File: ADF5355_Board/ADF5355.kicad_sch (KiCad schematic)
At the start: 20 parts

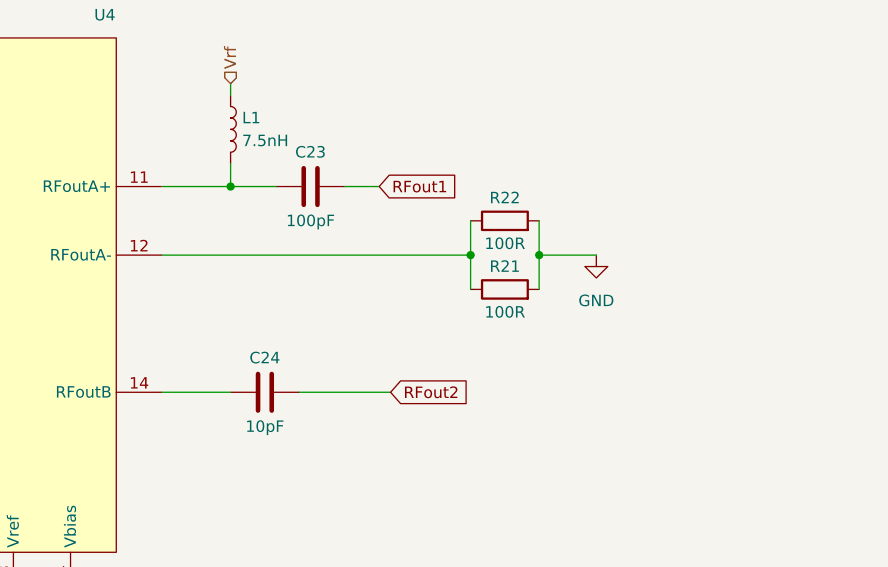
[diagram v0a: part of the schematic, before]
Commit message: Finished MCU board
Finished MCU board and started finishing up the VCO board
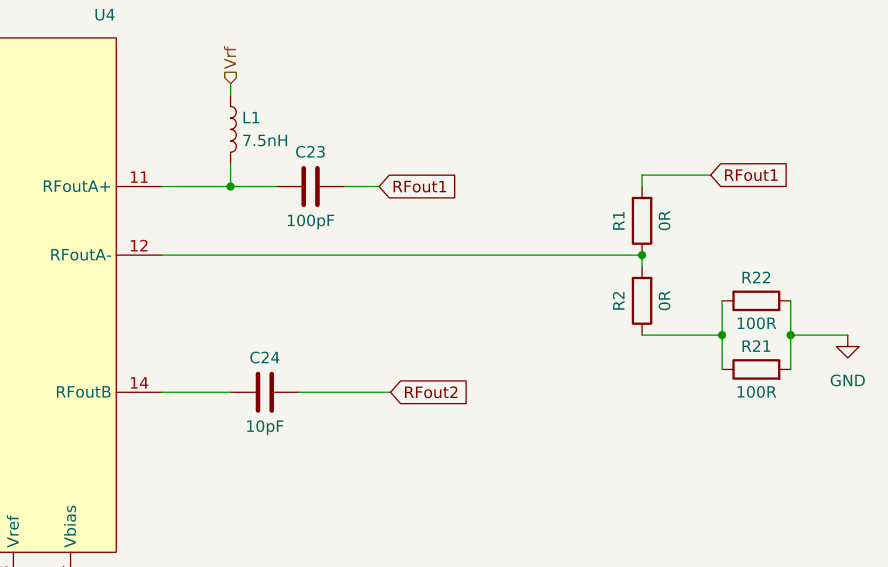
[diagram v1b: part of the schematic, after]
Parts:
- added R1, R2: 0R, symbol Device:R
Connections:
- net RFout1: now also R1.2
- net at R21.1, R22.1: now also R2.1; no longer U4.12 (RFoutA-)
- new net: R1.1, R2.2, U4.12 (RFoutA-)
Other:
- moved on the sheet: R21, R22
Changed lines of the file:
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@@
   (junction (at 156.21 139.7) (diameter 0) (color 0 0 0 0)
   )
-  (junction (at 219.71 85.09) (diameter 0) (color 0 0 0 0)
+  (junction (at 240.03 93.98) (diameter 0) (color 0 0 0 0)
+  )
+  (junction (at 247.65 93.98) (diameter 0) (color 0 0 0 0)
   )
   (junction (at 146.05 123.19) (diameter 0) (color 0 0 0 0)
@@
   (junction (at 185.42 77.47) (diameter 0) (color 0 0 0 0)
   )
+  (junction (at 231.14 85.09) (diameter 0) (color 0 0 0 0)
+  )
   (junction (at 138.43 123.19) (diameter 0) (color 0 0 0 0)
   )
@@
   (junction (at 140.97 123.19) (diameter 0) (color 0 0 0 0)
   )
-  (junction (at 212.09 85.09) (diameter 0) (color 0 0 0 0)
-  )
   (junction (at 54.61 101.6) (diameter 0) (color 0 0 0 0)
   )
@@
     (stroke (width 0) (type default))
   )
-  (wire (pts (xy 177.8 85.09) (xy 212.09 85.09))
-    (stroke (width 0) (type default))
-  )
   (wire (pts (xy 143.51 55.88) (xy 146.05 55.88))
     (stroke (width 0) (type default))
@@
     (stroke (width 0) (type default))
   )
+  (wire (pts (xy 231.14 86.36) (xy 231.14 85.09))
+    (stroke (width 0) (type default))
+  )
+  (wire (pts (xy 231.14 93.98) (xy 240.03 93.98))
+    (stroke (width 0) (type default))
+  )
   (wire (pts (xy 43.18 96.52) (xy 43.18 101.6))
     (stroke (width 0) (type default))
   )
-  (wire (pts (xy 219.71 85.09) (xy 226.06 85.09))
+  (wire (pts (xy 247.65 93.98) (xy 254 93.98))
     (stroke (width 0) (type default))
   )
@@
     (stroke (width 0) (type default))
   )
-  (wire (pts (xy 212.09 81.28) (xy 212.09 85.09))
-    (stroke (width 0) (type default))
-  )
-  (wire (pts (xy 219.71 81.28) (xy 219.71 85.09))
+  (wire (pts (xy 247.65 90.17) (xy 247.65 93.98))
     (stroke (width 0) (type default))
   )
@@
     (stroke (width 0) (type default))
   )
+  (wire (pts (xy 238.76 76.2) (xy 231.14 76.2))
+    (stroke (width 0) (type default))
+  )
   (wire (pts (xy 71.12 66.04) (xy 71.12 90.17))
     (stroke (width 0) (type default))
@@
     (stroke (width 0) (type default))
   )
-  (wire (pts (xy 212.09 85.09) (xy 212.09 88.9))
-    (stroke (width 0) (type default))
-  )
   (wire (pts (xy 181.61 139.7) (xy 181.61 135.89))
     (stroke (width 0) (type default))
@@
     (stroke (width 0) (type default))
   )
+  (wire (pts (xy 240.03 93.98) (xy 240.03 97.79))
+    (stroke (width 0) (type default))
+  )
   (wire (pts (xy 96.52 74.93) (xy 105.41 74.93))
     (stroke (width 0) (type default))
@@
     (stroke (width 0) (type default))
   )
-  (wire (pts (xy 219.71 85.09) (xy 219.71 88.9))
+  (wire (pts (xy 247.65 93.98) (xy 247.65 97.79))
     (stroke (width 0) (type default))
   )
@@
     (stroke (width 0) (type default))
   )
+  (wire (pts (xy 231.14 76.2) (xy 231.14 77.47))
+    (stroke (width 0) (type default))
+  )
   (wire (pts (xy 63.5 81.28) (xy 63.5 85.09))
     (stroke (width 0) (type default))
@@
     (stroke (width 0) (type default))
   )
+  (wire (pts (xy 231.14 85.09) (xy 177.8 85.09))
+    (stroke (width 0) (type default))
+  )
   (wire (pts (xy 130.81 46.99) (xy 135.89 46.99))
+    (stroke (width 0) (type default))
+  )
+  (wire (pts (xy 240.03 90.17) (xy 240.03 93.98))
     (stroke (width 0) (type default))
   )
@@
     (effects (font (size 1.27 1.27)) (justify left))
     (property "Intersheetrefs" "${INTERSHEET_REFS}" (at 212.0434 100.33 0)
+      (effects (font (size 1.27 1.27)) (justify left) hide)
+    )
+  )
+  (global_label "RFout1" (shape input) (at 238.76 76.2 0) (fields_autoplaced)
+    (effects (font (size 1.27 1.27)) (justify left))
+    (property "Intersheetrefs" "${INTERSHEET_REFS}" (at 247.6034 76.2 0)
       (effects (font (size 1.27 1.27)) (justify left) hide)
     )
@@
     )
   )
-  (symbol (lib_id "Device:R") (at 215.9 88.9 90) (unit 1)
-    (in_bom yes) (on_board yes) (dnp no)
-    (property "Reference" "R21" (at 215.9 86.36 90)
-      (effects (font (size 1.27 1.27)))
-    )
-    (property "Value" "100R" (at 215.9 91.44 90)
-      (effects (font (size 1.27 1.27)))
-    )
-    (property "Footprint" "Resistor_SMD:R_0603_1608Metric_Pad0.98x0.95mm_HandSolder" (at 215.9 90.678 90)
-      (effects (font (size 1.27 1.27)) hide)
-    )
-    (property "Datasheet" "~" (at 215.9 88.9 0)
+  (symbol (lib_id "Device:R") (at 243.84 97.79 90) (unit 1)
+    (in_bom yes) (on_board yes) (dnp no)
+    (property "Reference" "R21" (at 243.84 95.25 90)
+      (effects (font (size 1.27 1.27)))
+    )
+    (property "Value" "100R" (at 243.84 100.33 90)
+      (effects (font (size 1.27 1.27)))
+    )
+    (property "Footprint" "Resistor_SMD:R_0603_1608Metric_Pad0.98x0.95mm_HandSolder" (at 243.84 99.568 90)
+      (effects (font (size 1.27 1.27)) hide)
+    )
+    (property "Datasheet" "~" (at 243.84 97.79 0)
       (effects (font (size 1.27 1.27)) hide)
     )
@@
     )
   )
-  (symbol (lib_id "Device:R") (at 215.9 81.28 90) (unit 1)
-    (in_bom yes) (on_board yes) (dnp no)
-    (property "Reference" "R22" (at 215.9 78.74 90)
-      (effects (font (size 1.27 1.27)))
-    )
-    (property "Value" "100R" (at 215.9 83.82 90)
-      (effects (font (size 1.27 1.27)))
-    )
-    (property "Footprint" "Resistor_SMD:R_0603_1608Metric_Pad0.98x0.95mm_HandSolder" (at 215.9 83.058 90)
-      (effects (font (size 1.27 1.27)) hide)
-    )
-    (property "Datasheet" "~" (at 215.9 81.28 0)
+  (symbol (lib_id "Device:R") (at 243.84 90.17 90) (unit 1)
+    (in_bom yes) (on_board yes) (dnp no)
+    (property "Reference" "R22" (at 243.84 87.63 90)
+      (effects (font (size 1.27 1.27)))
+    )
+    (property "Value" "100R" (at 243.84 92.71 90)
+      (effects (font (size 1.27 1.27)))
+    )
+    (property "Footprint" "Resistor_SMD:R_0603_1608Metric_Pad0.98x0.95mm_HandSolder" (at 243.84 91.948 90)
+      (effects (font (size 1.27 1.27)) hide)
+    )
+    (property "Datasheet" "~" (at 243.84 90.17 0)
       (effects (font (size 1.27 1.27)) hide)
     )
@@
     )
   )
-  (symbol (lib_id "power:GND") (at 226.06 85.09 0) (unit 1)
-    (in_bom yes) (on_board yes) (dnp no) (fields_autoplaced)
-    (property "Reference" "#PWR034" (at 226.06 91.44 0)
-      (effects (font (size 1.27 1.27)) hide)
-    )
-    (property "Value" "GND" (at 226.06 90.17 0)
-      (effects (font (size 1.27 1.27)))
-    )
-    (property "Footprint" "" (at 226.06 85.09 0)
-      (effects (font (size 1.27 1.27)) hide)
-    )
-    (property "Datasheet" "" (at 226.06 85.09 0)
+  (symbol (lib_id "power:GND") (at 254 93.98 0) (unit 1)
+    (in_bom yes) (on_board yes) (dnp no) (fields_autoplaced)
+    (property "Reference" "#PWR034" (at 254 100.33 0)
+      (effects (font (size 1.27 1.27)) hide)
+    )
+    (property "Value" "GND" (at 254 99.06 0)
+      (effects (font (size 1.27 1.27)))
+    )
+    (property "Footprint" "" (at 254 93.98 0)
+      (effects (font (size 1.27 1.27)) hide)
+    )
+    (property "Datasheet" "" (at 254 93.98 0)
       (effects (font (size 1.27 1.27)) hide)
     )
@@
     )
   )
+  (symbol (lib_id "Device:R") (at 231.14 81.28 180) (unit 1)
+    (in_bom yes) (on_board yes) (dnp no)
+    (property "Reference" "R1" (at 228.6 81.28 90)
+      (effects (font (size 1.27 1.27)))
+    )
+    (property "Value" "0R" (at 233.68 81.28 90)
+      (effects (font (size 1.27 1.27)))
+    )
+    (property "Footprint" "" (at 232.918 81.28 90)
+      (effects (font (size 1.27 1.27)) hide)
+    )
+    (property "Datasheet" "~" (at 231.14 81.28 0)
+      (effects (font (size 1.27 1.27)) hide)
+    )
+    (pin "1")
+    (pin "2")
+    (instances
+      (project "ADF5355_Board"
+        (path "/29349b68-071c-451b-9b1e-10b5ef7e12a6/ea810e70-e3dc-4641-ad7c-8ecf7484ded2"
+          (reference "R1") (unit 1)
+        )
+      )
+    )
+  )
   (symbol (lib_id "Device:FerriteBead") (at 127 46.99 90) (unit 1)
     (in_bom yes) (on_board yes) (dnp no) (fields_autoplaced)
@@
         )
       )
+    )
+  )
+  (symbol (lib_id "Device:R") (at 231.14 90.17 180) (unit 1)
+    (in_bom yes) (on_board yes) (dnp no)
+    (property "Reference" "R2" (at 228.6 90.17 90)
+      (effects (font (size 1.27 1.27)))
+    )
+    (property "Value" "0R" (at 233.68 90.17 90)
+      (effects (font (size 1.27 1.27)))
+    )
+    (property "Footprint" "" (at 232.918 90.17 90)
+      (effects (font (size 1.27 1.27)) hide)
+    )
+    (property "Datasheet" "~" (at 231.14 90.17 0)
+      (effects (font (size 1.27 1.27)) hide)
+    )
+    (pin "1")
+    (pin "2")
+    (instances
+      (project "ADF5355_Board"
+        (path "/29349b68-071c-451b-9b1e-10b5ef7e12a6/ea810e70-e3dc-4641-ad7c-8ecf7484ded2"
+          (reference "R2") (unit 1)
+        )
+      )

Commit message: IDK where I stopped
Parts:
- added C11, C12, C13, C14, C15, C16: 100nF, Capacitor_SMD:C_0402_1005Metric_Pad0.74x0.62mm_HandSolder, symbol Device:C_Small
- C25, C26, C27, C28, C29, C30, C31, C32: footprint Capacitor_SMD:C_0603_1608Metric_Pad1.08x0.95mm_HandSolder -> Capacitor_SMD:C_0402_1005Metric_Pad0.74x0.62mm_HandSolder
- R1, R2, R29, R30, R31, R41: footprint (none) -> Capacitor_SMD:C_0402_1005Metric_Pad0.74x0.62mm_HandSolder
- U4: footprint ADF5355_footprint_lib:162K-CC_BC-3LP -> ADF5355_footprint_lib:QFN-32_EP_5x5_Pitch0.5mm
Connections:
- net +3V3: now also C11.1, C12.1, C13.1
- net +5V: now also C14.1, C15.1, C16.1
- net GND: now also C11.2, C12.2, C13.2, C14.2, C15.2, C16.2
- net RFout1: no longer R1.2
- net RFout2: now also R1.2; no longer C24.2
- new net RFout3: C24.2
